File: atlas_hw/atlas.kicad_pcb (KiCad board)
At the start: 4 copper layers, 147 parts, among them J1 USB_B_Micro, J10 PSP_LCD, J2 DEBUG_STM, J3 PSP_TOUCH, J4 UPDI_DSS, J5 EXP_L, J6 EXP_R, J8 Micro_SD_Card_Det, J9 PSP_LCD_BL, Q1 Q_NMOS_DGS, Q2 Q_NMOS_DGS, Q4 Q_NMOS_DGS, SW1 BTN_L_EXT, SW2 BTN_0_EXT, SW3 ResetSTM, SW4 BTN_R_EXT, SW5 BTN_PWR_EXT, U1 STM32H723VITx, U11 L96-M33, U13 LSF0108, U14 NPP600SNADJ, U16 PAM2841, U2 S27KL0641DABHV023, U3 MCP1811B, U4 TLV62569DBV, U5 MX25L3233FM2I-08G, U6 ST1PS02, U7 ATtiny402-SS, U9 MC6470, Y1 16M, Y4 32k

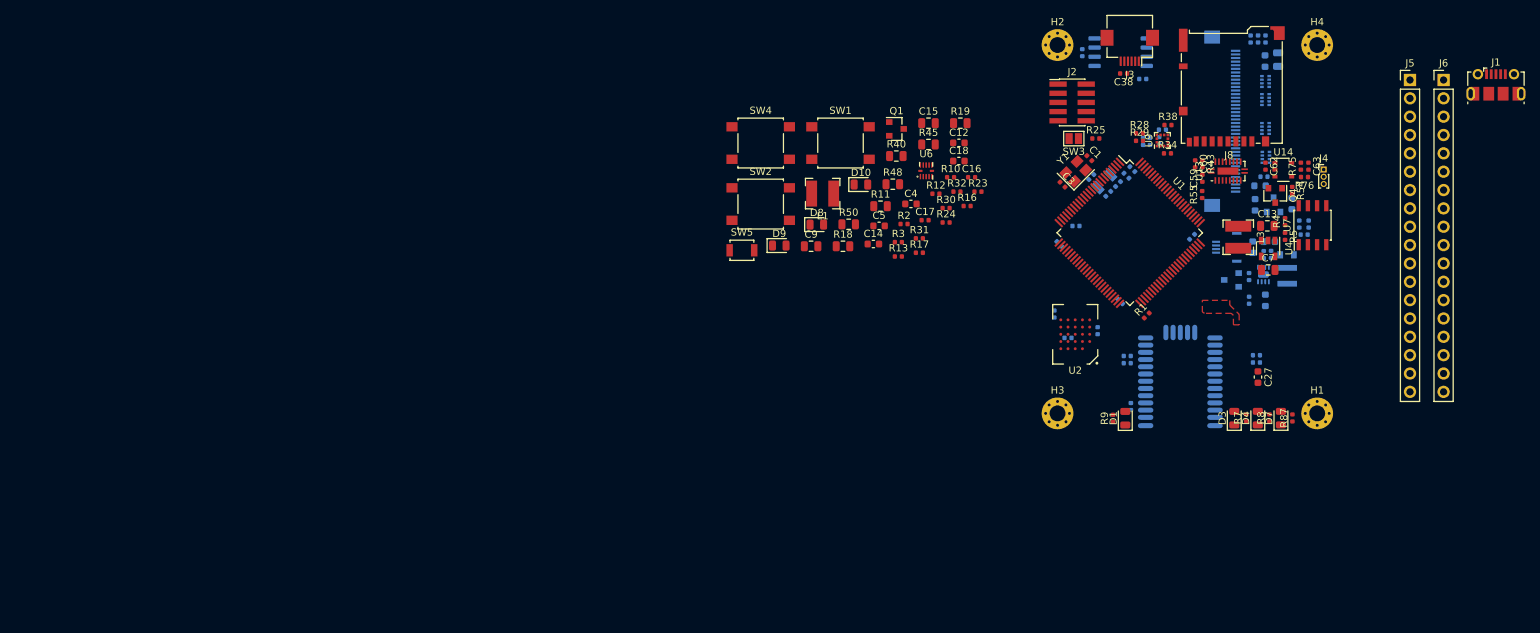
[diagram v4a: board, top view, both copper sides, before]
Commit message: dfm reductions
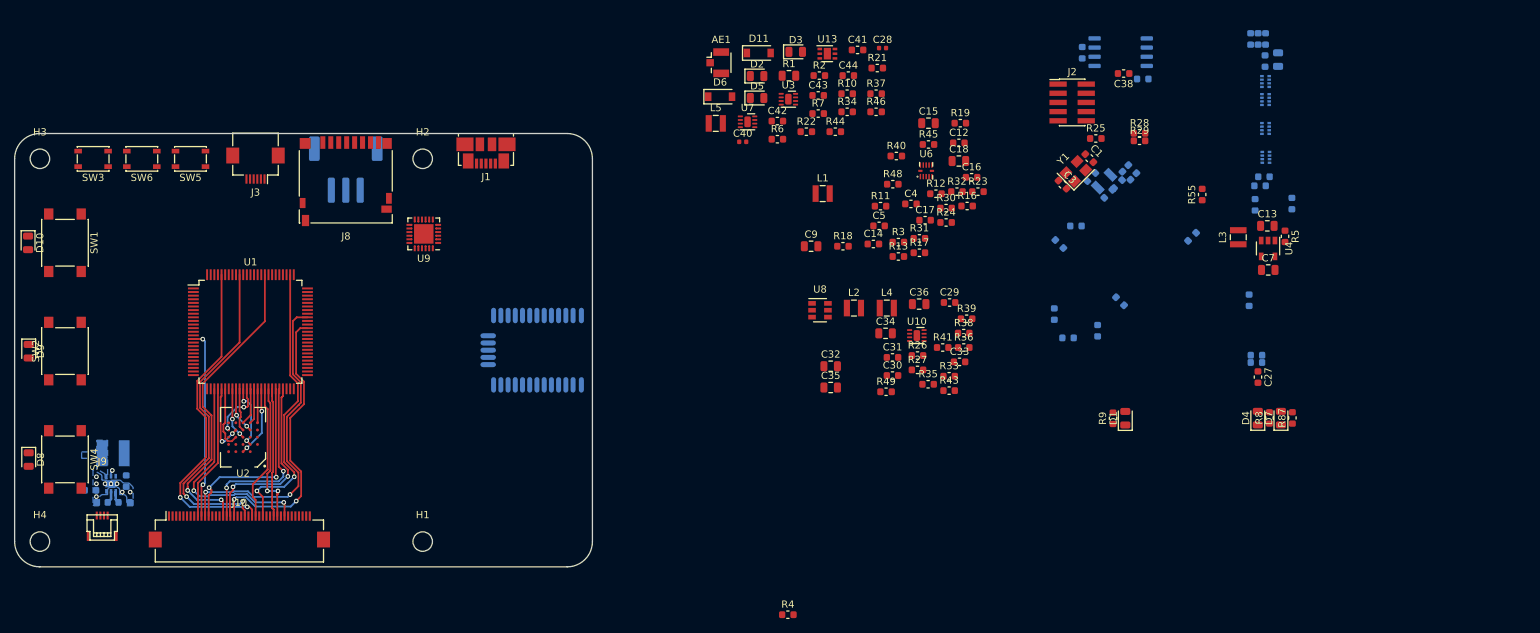
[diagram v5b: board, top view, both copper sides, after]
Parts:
- removed C48: 1u, Capacitor_SMD:C_0603_1608Metric
- removed C49, C59, C60: 0.1u, Capacitor_SMD:C_0402_1005Metric
- removed C62, C63: 1u, Capacitor_SMD:C_0402_1005Metric
- removed J4: UPDI_DSS, Connector_PinHeader_1.00mm:PinHeader_1x03_P1.00mm_Vertical
- removed J6: EXP_R, Connector_PinHeader_2.54mm:PinHeader_1x18_P2.54mm_Vertical
- removed Q1, Q2, Q4: Q_NMOS_DGS, Package_TO_SOT_SMD:SOT-23
- removed R50: 100k, Resistor_SMD:R_0805_2012Metric
- removed R54: 10k, Resistor_SMD:R_0402_1005Metric
- removed R75: 200k, Resistor_SMD:R_0402_1005Metric
- removed R76: 250k, Resistor_SMD:R_0402_1005Metric
- removed R78, R79: 4.7k, Resistor_SMD:R_0402_1005Metric
- removed U14: NPP600SNADJ, Package_SO:TSOP-5_1.65x3.05mm_P0.95mm
- removed U16: PAM2841, Package_DFN_QFN:DFN-8-1EP_2x2mm_P0.5mm_EP0.9x1.5mm
- added AE1: Antenna_Shield, Connector_Coaxial:U.FL_Hirose_U.FL-R-SMT-1_Vertical, F.Cu at (131.0, 90.2)
- added C29: 1u, Capacitor_SMD:C_0603_1608Metric, F.Cu at (163.1, 123.4)
- added C30: 1u, Capacitor_SMD:C_0603_1608Metric, F.Cu at (155.2, 133.5)
- added C31: 1u, Capacitor_SMD:C_0603_1608Metric, F.Cu at (155.2, 131.0)
- added C33: 0.1u, Capacitor_SMD:C_0603_1608Metric, F.Cu at (164.5, 131.6)
- added C35: 10u, Capacitor_SMD:C_0805_2012Metric, F.Cu at (146.6, 135.2)
- added C36: 10u, Capacitor_SMD:C_0805_2012Metric, F.Cu at (158.9, 123.6)
- added C37: 1u, Capacitor_SMD:C_0603_1608Metric, B.Cu at (49.1, 148.1)
- added C39: 0.1u, Capacitor_SMD:C_0603_1608Metric, B.Cu at (45.8, 151.1)
- added C40: NP, Capacitor_SMD:C_0402_1005Metric, F.Cu at (134.5, 101.2)
- added C41: 4.7u, Capacitor_SMD:C_0603_1608Metric, F.Cu at (150.4, 88.4)
- added C42: 1u, Capacitor_SMD:C_0603_1608Metric, F.Cu at (139.3, 98.3)
- added C43: 1u, Capacitor_SMD:C_0603_1608Metric, F.Cu at (144.9, 94.7)
- added C44: 1u, Capacitor_SMD:C_0603_1608Metric, F.Cu at (149.1, 92.0)
- added D11: MBR0540, Diode_SMD:D_SOD-123, F.Cu at (136.7, 88.8)
- added D2: GPS_3DF, LED_SMD:LED_0805_2012Metric, F.Cu at (136.4, 92.0)
- added D5: GPS_JAM, LED_SMD:LED_0805_2012Metric, F.Cu at (136.4, 95.1)
- added L2: 2.2u, Inductor_SMD:L_Wuerth_MAPI-2510, F.Cu at (149.9, 124.2)
- added L4: 2.2u, Inductor_SMD:L_Wuerth_MAPI-2510, F.Cu at (154.4, 124.2)
- added L5: 47n, Inductor_SMD:L_Wuerth_MAPI-2510, F.Cu at (130.7, 98.6)
- added R33: 0, Resistor_SMD:R_0603_1608Metric, F.Cu at (163.0, 133.6)
- added R35: 100k, Resistor_SMD:R_0603_1608Metric, F.Cu at (160.1, 134.7)
- added R36: 100k, Resistor_SMD:R_0603_1608Metric, F.Cu at (165.1, 129.6)
- added R37: 440k, Resistor_SMD:R_0603_1608Metric, F.Cu at (152.9, 94.5)
- added R41: 0, Resistor_SMD:R_0603_1608Metric, F.Cu at (162.2, 129.6)
- added R46: 100k, Resistor_SMD:R_0603_1608Metric, F.Cu at (152.9, 97.0)
- added R49: 100k, Resistor_SMD:R_0603_1608Metric, F.Cu at (154.3, 135.8)
- added SW6: BTN_BOOT, Button_Switch_SMD:SW_SPST_PTS810, F.Cu at (51.3, 103.5)
- added U10: MAX17048, Package_DFN_QFN:DFN-8-1EP_2x2mm_P0.5mm_EP0.9x1.5mm, F.Cu at (158.6, 128.0)
- added U12: LV52204MU, Package_DFN_QFN:DFN-6-1EP_2x2mm_P0.65mm_EP1x1.6mm, B.Cu at (47.0, 148.5)
- added U8: MCP1640B, Package_TO_SOT_SMD:SOT-23-6, F.Cu at (145.2, 124.5)
- C1, C11, C16, C17, C2, C22, C23, C24, C25, C26, C3, C38, C54, C56, C57, C58, C6: footprint Capacitor_SMD:C_0402_1005Metric -> Capacitor_SMD:C_0603_1608Metric
- C18: footprint Capacitor_SMD:C_0603_1608Metric -> Capacitor_SMD:C_0805_2012Metric
- C19, C21: value 22p -> 18p; footprint Capacitor_SMD:C_0402_1005Metric -> Capacitor_SMD:C_0603_1608Metric
- C28: value 0.1u -> NP; moved to F.Cu
- C32: value 0.1u -> 10u; footprint Capacitor_SMD:C_0402_1005Metric -> Capacitor_SMD:C_0805_2012Metric; moved to F.Cu
- C34: value 0.1u -> 4.7u; footprint Capacitor_SMD:C_0402_1005Metric -> Capacitor_SMD:C_0805_2012Metric; moved to F.Cu
- C7: value 10u -> 4.7u
- C8: value 1u -> 4.7u
- D3: value GPS_3DF -> CHG_STATUS
- D6: value D_Schottky_Small_ALT -> MBR0540; footprint Diode_SMD:D_SOD-110 -> Diode_SMD:D_SOD-123; moved to F.Cu
- H1, H2, H3, H4: value MountingHole_Pad -> MountingHole; footprint MountingHole:MountingHole_2.2mm_M2_Pad_Via -> MountingHole:MountingHole_2.7mm_M2.5
- J1: footprint Connector_USB:USB_Micro-B_Molex-105017-0001 -> Connector_USB:USB_Micro-B_Molex_47346-0001
- J10, J9: moved to F.Cu
- J5: value EXP_L -> CELL; footprint Connector_PinHeader_2.54mm:PinHeader_1x18_P2.54mm_Vertical -> Connector_JST:JST_PH_S3B-PH-SM4-TB_1x03-1MP_P2.00mm_Horizontal; moved to B.Cu
- J8: footprint Connector_Card:microSD_HC_Hirose_DM3BT-DSF-PEJS -> Connector_Card:microSD_HC_Hirose_DM3D-SF
- L1: footprint Inductor_SMD:L_Bourns-SRN4018 -> Inductor_SMD:L_Wuerth_MAPI-2510
- L10: value 3.9n -> 22u; footprint Inductor_SMD:L_Taiyo-Yuden_MD-3030 -> Inductor_SMD:L_Bourns-SRN4018
- L3: value L_Small -> 2.2u; footprint Inductor_SMD:L_Bourns-SRN4018 -> Inductor_SMD:L_Wuerth_MAPI-2510
- R1: value 100k -> 0; footprint Resistor_SMD:R_0402_1005Metric -> Resistor_SMD:R_0805_2012Metric
- R10: value 100k -> NP; footprint Resistor_SMD:R_0402_1005Metric -> Resistor_SMD:R_0603_1608Metric
- R11, R18, R19, R40, R45, R48: footprint Resistor_SMD:R_0805_2012Metric -> Resistor_SMD:R_0603_1608Metric
- R12, R13, R14, R15, R16, R17, R23, R24, R25, R30, R31, R32, R34, R42, R47, R5, R55, R7, R8, R82, R83, R84, R87, R9: footprint Resistor_SMD:R_0402_1005Metric -> Resistor_SMD:R_0603_1608Metric
- R2: value 100k -> 1k; footprint Resistor_SMD:R_0402_1005Metric -> Resistor_SMD:R_0603_1608Metric
- R21: footprint Resistor_SMD:R_0402_1005Metric -> Resistor_SMD:R_0603_1608Metric; moved to F.Cu
- R22: value 0 -> 100k; footprint Resistor_SMD:R_0402_1005Metric -> Resistor_SMD:R_0603_1608Metric; moved to F.Cu
- R26: value NP -> 450; footprint Resistor_SMD:R_0402_1005Metric -> Resistor_SMD:R_0603_1608Metric; moved to F.Cu
- R27: value NP -> 240; footprint Resistor_SMD:R_0402_1005Metric -> Resistor_SMD:R_0603_1608Metric; moved to F.Cu
- R28, R29: value 4.7k -> 5.7k; footprint Resistor_SMD:R_0402_1005Metric -> Resistor_SMD:R_0603_1608Metric
- R3, R43: value 100k -> 0; footprint Resistor_SMD:R_0402_1005Metric -> Resistor_SMD:R_0603_1608Metric
- R38: value 100k -> 5.7k; footprint Resistor_SMD:R_0402_1005Metric -> Resistor_SMD:R_0603_1608Metric
- R39: value 0 -> 30k; footprint Resistor_SMD:R_0402_1005Metric -> Resistor_SMD:R_0603_1608Metric; moved to F.Cu
- R4: value 200k -> 100k; footprint Resistor_SMD:R_0402_1005Metric -> Resistor_SMD:R_0603_1608Metric
- R44: value 100k -> 10; footprint Resistor_SMD:R_0402_1005Metric -> Resistor_SMD:R_0603_1608Metric; moved to F.Cu
- R6: value 100k -> 1k; footprint Resistor_SMD:R_0402_1005Metric -> Resistor_SMD:R_0603_1608Metric; moved to F.Cu
- SW1: value BTN_L_EXT -> BTN_L; footprint Button_Switch_SMD:SW_SPST_B3S-1000 -> Button_Switch_SMD:SW_SPST_PTS645
- SW2: value BTN_0_EXT -> BTN_0; footprint Button_Switch_SMD:SW_SPST_B3S-1000 -> Button_Switch_SMD:SW_SPST_PTS645
- SW3: footprint Jumper:SolderJumper-2_P1.3mm_Open_Pad1.0x1.5mm -> Button_Switch_SMD:SW_SPST_PTS810
- SW4: value BTN_R_EXT -> BTN_R; footprint Button_Switch_SMD:SW_SPST_B3S-1000 -> Button_Switch_SMD:SW_SPST_PTS645
- SW5: value BTN_PWR_EXT -> BTN_PWR; footprint Button_Switch_SMD:SW_SPST_B3U-1000P -> Button_Switch_SMD:SW_SPST_PTS810
- U1: value STM32H723VITx -> STM32H723VGT6
- U13: value LSF0108 -> AP22804; footprint Package_DFN_QFN:WQFN-20-1EP_2.5x4.5mm_P0.5mm_EP1x2.9mm -> Package_DFN_QFN:DFN-6-1EP_2x2mm_P0.65mm_EP1x1.6mm
- U3: value MCP1811B -> MCP1810; footprint Package_TO_SOT_SMD:SOT-23 -> Package_DFN_QFN:DFN-8-1EP_2x2mm_P0.5mm_EP0.9x1.5mm; moved to F.Cu
- U7: value ATtiny402-SS -> MCP1810; footprint Package_SO:SOIC-8_3.9x4.9mm_P1.27mm -> Package_DFN_QFN:DFN-8-1EP_2x2mm_P0.5mm_EP0.9x1.5mm
- U9: value MC6470 -> BQ25606; footprint Package_LGA:LGA-12_2x2mm_P0.5mm -> Package_DFN_QFN:WQFN-24-1EP_4x4mm_P0.5mm_EP2.7x2.7mm
- Y1: value 16M -> 8M
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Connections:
- net /DSS_EXT renamed Net-(U7-Pad5)
- C1 pad 1: GND -> EP
- C10 pad 1: GND -> EP
- C11 pad 1: /VCC_3V3 -> Net-(C11-Pad1)
- C11 pad 2: GND -> EP
- C12 pad 2: GND -> EP
- C13 pad 1: /VCC_3V3 -> /VCC_3V3_MCU
- C13 pad 2: GND -> EP
- C14 pad 2: GND -> EP
- C15 pad 2: GND -> EP
- C16 pad 2: GND -> EP
- C17 pad 2: GND -> EP
- C18 pad 2: GND -> EP
- C19 pad 1: GND -> EP
- C2 pad 1: GND -> EP
- C2 pad 2: /VCC_3V3 -> /VCC_3V3_PERIPH
- C20 pad 1: /VCC_MCU_3V3 -> /VCC_3V3_PERIPH
- C20 pad 2: GND -> EP
- C21 pad 1: GND -> EP
- C22 pad 1: /VCC_3V3 -> /VCC_3V3_MCU
- C22 pad 2: GND -> EP
- C23 pad 1: /VCC_3V3 -> /VCC_3V3_MCU
- C23 pad 2: GND -> EP
- C24 pad 1: /VCC_3V3 -> /VCC_3V3_MCU
- C24 pad 2: GND -> EP
- C25 pad 1: /VCC_3V3 -> /VCC_3V3_MCU
- C25 pad 2: GND -> EP
- C26 pad 1: /VCC_3V3 -> /VCC_3V3_MCU
- C26 pad 2: GND -> EP
- C27 pad 2: GND -> EP
- C28 pad 1: GND -> EP
- C28 pad 2: /VCC_BACKUP -> Net-(C28-Pad2)
- C3 pad 1: GND -> EP
- C32 pad 1: /VCC_3V3 -> Net-(C32-Pad1)
- C32 pad 2: GND -> EP
- C34 pad 1: /VCC_3V3 -> Net-(C34-Pad1)
- C34 pad 2: GND -> EP
- C38 pad 1: /VCC_MCU_3V3 -> /VCC_3V3_PERIPH
- C38 pad 2: GND -> EP
- C4 pad 2: GND -> EP
- C5 pad 2: GND -> EP
- C51 pad 1: /VCC_SYS -> /VCC_LCD_PWR
- C51 pad 2: GND -> EP
- C52 pad 1: GND -> EP
- C52 pad 2: Net-(C52-Pad2) -> /BL_HV
- C53 pad 1: /VCC_SYS -> /VCC_LCD_PWR
- C53 pad 2: GND -> EP
- C54 pad 1: /VCC_MCU_3V3 -> /VCC_3V3_PERIPH
- C54 pad 2: GND -> EP
- C56 pad 1: GND -> EP
- C56 pad 2: /VCC_3V3 -> /VCC_3V3_PERIPH
- C57 pad 1: GND -> EP
- C57 pad 2: /VCC_3V3 -> /VCC_3V3_PERIPH
- C58 pad 1: GND -> EP
- C58 pad 2: /VCC_3V3 -> /VCC_3V3_PERIPH
- C6 pad 2: GND -> EP
- C7 pad 2: GND -> EP
- C8 pad 1: GND -> EP
- C9 pad 1: /VCC_SYS -> Net-(C9-Pad1)
- C9 pad 2: GND -> EP
- D10 pad 1: GND -> EP
- D3 pad 2: /GPS_3DF -> /VCC_BACKUP
- D6 pad 1: Net-(C52-Pad2) -> /VCC_3V3_MCU_EN
- D6 pad 2: Net-(D6-Pad2) -> /SW_PWR
- D8 pad 1: GND -> EP
- D9 pad 1: GND -> EP
- H1 pad 1: GND -> (no net)
- H2 pad 1: GND -> (no net)
- H3 pad 1: GND -> (no net)
- H4 pad 1: GND -> (no net)
- J1 pad 2: /USB_PORT_D- -> /USB_PORT_D+
- J1 pad 3: /USB_PORT_D+ -> /USB_PORT_D-
- J1 pad 5: GND -> EP
- J1 pad 6: GND -> EP
- J10 pad 35: /VCC_SYS -> /VCC_LCD_PWR
- J10 pad 36: /VCC_SYS -> /VCC_LCD_PWR
- J2 pad 1: /VCC_3V3 -> /VCC_3V3_MCU
- J2 pad 3: GND -> EP
- J2 pad 5: GND -> EP
- J2 pad 9: GND -> EP
- J3 pad 1: /I2C1_SCL_SENSOR -> /I2C4_SCL_SENSOR_PB6
- J3 pad 2: /I2C1_SDA_SENSOR -> /I2C4_SCL_SENSOR_PB7
- J3 pad 3: /STC911_INT -> /TOUCH_INT
- J3 pad 6: /STC911_RESET -> /DEBUG_NRESET_STM
- J5 pad 1: /USB_PORT_VBUS -> GND
- J5 pad 2: /VCC_SYS -> /CELL_NTC
- J5 pad 3: /VCC_BACKUP -> /CELL_POS
- J8 pad 10: GND -> /SD_DET
- J8 pad 9: /SD_DET -> GND
- J9 pad 1: Net-(C52-Pad2) -> /BL_HV
- L10 pad 2: Net-(D6-Pad2) -> Net-(D11-Pad2)
- L3 pad 2: /VCC_3V3 -> /VCC_3V3_MCU
- R1 pad 1: /VCC_MCU_3V3 -> Net-(C11-Pad1)
- R1 pad 2: /PWR_ACK_DSS -> /VCC_3V3_MCU
- R10 pad 1: /STM_VCORE_GOOD -> /VCC_SYS
- R10 pad 2: /VCC_MCU_3V3 -> Net-(C9-Pad1)
- R14 pad 1: /USB_STM_D+ -> /USB_STM_D-
- R14 pad 2: /USB_PORT_D+ -> /USB_PORT_D-
- R15 pad 1: /USB_STM_D- -> /USB_STM_D+
- R15 pad 2: /USB_PORT_D- -> /USB_PORT_D+
- R18 pad 1: /STM_STATUS_0 -> /STM_STATUS_C
- R2 pad 1: /PWR_EN_O -> Net-(D2-Pad1)
- R2 pad 2: /VCORE_EN -> EP
- R21 pad 1: Net-(R21-Pad1) -> /VCC_3V3_MCU
- R21 pad 2: /VCC_MCU_3V3 -> Net-(C9-Pad1)
- R22 pad 1: Net-(R21-Pad1) -> /SW_PWR
- R22 pad 2: /DEBUG_NRESET_STM -> EP
- R25 pad 2: /VCC_3V3 -> /VCC_3V3_MCU
- R26 pad 1: GND -> Net-(R26-Pad1)
- R26 pad 2: Net-(R26-Pad2) -> EP
- R27 pad 1: Net-(R26-Pad2) -> Net-(R27-Pad1)
- R27 pad 2: /VCC_MCU_3V3 -> EP
- R28 pad 1: /VCC_MCU_3V3 -> /VCC_3V3_PERIPH
- R28 pad 2: /I2C1_SCL_SENSOR -> /I2C4_SCL_SENSOR_PB6
- R29 pad 1: /VCC_MCU_3V3 -> /VCC_3V3_PERIPH
- R29 pad 2: /I2C1_SDA_SENSOR -> /I2C4_SCL_SENSOR_PB7
- R3 pad 1: GND -> EP
- R34 pad 1: /VCC_MCU_3V3 -> /STM_VCORE_GOOD
- R34 pad 2: /MC6470_INTA -> /VCC_CORE
- R38 pad 1: /VCC_MCU_3V3 -> Net-(C34-Pad1)
- R38 pad 2: /MC6470_INTM -> /CELL_NTC
- R39 pad 1: Net-(R39-Pad1) -> /CELL_NTC
- R39 pad 2: Net-(R39-Pad2) -> EP
- R4 pad 1: Net-(R4-Pad1) -> /VCC_3V3
- R4 pad 2: /VCC_3V3 -> /SW_BOOT
- R42 pad 1: /VCC_MCU_3V3 -> /VCC_3V3_PERIPH
- R42 pad 2: /STC911_INT -> /TOUCH_INT
- R43 pad 1: /VDD_SD_IO_3V3_1V8 -> /USB_CHG_D+
- R43 pad 2: Net-(R43-Pad2) -> /USB_PORT_D+
- R44 pad 1: /VCC_BACKUP -> Net-(C42-Pad2)
- R44 pad 2: /PWR_EN_O -> Net-(L5-Pad2)
- R45 pad 2: /SW_0 -> /SW_C
- R47 pad 1: GND -> EP
- R47 pad 2: /EN_LCD_PWR -> /T3C1_LCD_BL
- R5 pad 1: GND -> EP
- R5 pad 2: Net-(R4-Pad1) -> Net-(R37-Pad1)
- R55 pad 2: /VCC_MCU_3V3 -> /VCC_3V3_PERIPH
- R6 pad 1: /PWR_EN_O -> Net-(D3-Pad1)
- R6 pad 2: GND -> /CHG_STATUS
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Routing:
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- added copper zone on B.Cu, net EP
- added copper zone on B.Cu, net Net-(D11-Pad2)
- removed copper zone on F.Cu, net Net-(C41-Pad1)
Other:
- board outline added: 80 x 60 mm

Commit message: lots of modifications to sch and board
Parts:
- added C45: 10u, Capacitor_SMD:C_0805_2012Metric, B.Cu at (90.2, 143.0)
- added C46: 0.1u, Capacitor_SMD:C_0402_1005Metric, F.Cu at (180.4, 122.1)
- added C47: 0.1u, Capacitor_SMD:C_0402_1005Metric, F.Cu at (188.3, 119.1)
- added C48: 0.1u, Capacitor_SMD:C_0402_1005Metric, F.Cu at (136.6, 93.7)
- added C49: 1u, Capacitor_SMD:C_0603_1608Metric, F.Cu at (143.0, 81.3)
- added C50: 1u, Capacitor_SMD:C_0603_1608Metric, F.Cu at (137.7, 89.2)
- added C55: 1u, Capacitor_SMD:C_0603_1608Metric, F.Cu at (125.8, 92.5)
- added C59: 0.1u, Capacitor_SMD:C_0402_1005Metric, F.Cu at (143.0, 83.3)
- added C60: 0.1u, Capacitor_SMD:C_0402_1005Metric, F.Cu at (133.7, 93.7)
- added C61: 0.1u, Capacitor_SMD:C_0402_1005Metric, F.Cu at (136.6, 91.7)
- added C62: 10n, Capacitor_SMD:C_0402_1005Metric, F.Cu at (143.0, 85.3)
- added C63: 0.1u, Capacitor_SMD:C_0402_1005Metric, F.Cu at (140.6, 89.2)
- added C64: 0.1u, Capacitor_SMD:C_0402_1005Metric, F.Cu at (133.7, 91.7)
- added C65: 0.1u, Capacitor_SMD:C_0402_1005Metric, F.Cu at (139.5, 91.2)
- added J4: DEBUG_NCP, Connector_PinHeader_1.27mm:PinHeader_2x05_P1.27mm_Vertical_SMD, B.Cu at (47.1, 151.5)
- added JP2: Jumper_NO_Small, Connector_PinHeader_1.00mm:PinHeader_1x02_P1.00mm_Vertical, F.Cu at (135.2, 53.4)
- added L6: FERRITE, Inductor_SMD:L_0603_1608Metric, F.Cu at (140.4, 148.8)
- added R50: 0, Resistor_SMD:R_0402_1005Metric, F.Cu at (99.1, 115.4)
- added R51: 0, Resistor_SMD:R_0402_1005Metric, F.Cu at (109.4, 122.5)
- added RV1: 200k, Potentiometer_SMD:Potentiometer_Bourns_3314J_Vertical, F.Cu at (136.6, 48.1)
- added SW7: NP, Button_Switch_SMD:SW_SPST_PTS645, F.Cu at (43.3, 129.9)
- added TP1: VCC_CORE, TestPoint:TestPoint_Bridge_Pitch2.0mm_Drill0.7mm, F.Cu at (172.2, 119.3)
- added U14: MS5637, atlas:QFN-4_3x3_Pitch2mm, F.Cu at (61.7, 115.6)
- added U15: SHT4x, atlas:SHT_QFN-4-1EP_1.5x1.5mm, F.Cu at (61.8, 110.8)
- added U16: PSP_JOY, atlas:PSP-JOY, F.Cu at (43.2, 130.0)
- added U17: BGM220P, atlas:BGM220P, B.Cu at (41.6, 130.0)
- added U18: FXOS8700CQ, atlas:LGA-16_3x3mm_P0.5mm_LayoutBorder3x5y, B.Cu at (55.2, 113.2)
- added U19: L2G2IS, atlas:LGA-16_2.3x2.3mm_P0.4mm_LayoutBorder3x5y, B.Cu at (48.0, 113.2)
- added U20: AZ2117, Package_TO_SOT_SMD:SOT-223-3_TabPin2, F.Cu at (62.0, 80.1)
- C1, C13, C3, C35, C36, C42, C43, C7, D11, J1, J2, L1, L2, L3, L4, R3, R34, R36, R37, R41, R43, R44, R5, U10, U13, U2, U3, U4, U6, U7, U8, U9: moved to B.Cu
- C11, C22, C23, C24, C25, C26, C56, C57, C58, C6: footprint Capacitor_SMD:C_0603_1608Metric -> Capacitor_SMD:C_0402_1005Metric; moved to F.Cu
- C16, C17, C2, C38, C39, C54: footprint Capacitor_SMD:C_0603_1608Metric -> Capacitor_SMD:C_0402_1005Metric
- C19, C21, R14, R15, U11: moved to F.Cu
- C29: value 1u -> 10u; footprint Capacitor_SMD:C_0603_1608Metric -> Capacitor_SMD:C_0805_2012Metric
- C30: value 1u -> 0.1u; footprint Capacitor_SMD:C_0603_1608Metric -> Capacitor_SMD:C_0402_1005Metric
- C31: value 1u -> 4.7u; footprint Capacitor_SMD:C_0603_1608Metric -> Capacitor_SMD:C_0805_2012Metric; moved to B.Cu
- C33: footprint Capacitor_SMD:C_0603_1608Metric -> Capacitor_SMD:C_0402_1005Metric; moved to B.Cu
- C41: footprint Capacitor_SMD:C_0603_1608Metric -> Capacitor_SMD:C_0805_2012Metric; moved to B.Cu
- C44: value 1u -> 10u; footprint Capacitor_SMD:C_0603_1608Metric -> Capacitor_SMD:C_0805_2012Metric; moved to B.Cu
- C8: footprint Capacitor_SMD:C_0603_1608Metric -> Capacitor_SMD:C_0805_2012Metric
- D5: value GPS_JAM -> NP
- D9: value STM_STATUS_0 -> PERIPH_FAULT
- H1, H2, H3, H4: footprint MountingHole:MountingHole_2.7mm_M2.5 -> MountingHole:MountingHole_2.7mm_M2.5_Pad_Via
- J5: footprint Connector_JST:JST_PH_S3B-PH-SM4-TB_1x03-1MP_P2.00mm_Horizontal -> Connector_PinHeader_1.27mm:PinHeader_1x03_P1.27mm_Vertical
- L5: footprint Inductor_SMD:L_Wuerth_MAPI-2510 -> Inductor_SMD:L_0402_1005Metric; moved to B.Cu
- R1: value 0 -> 1k; footprint Resistor_SMD:R_0805_2012Metric -> Resistor_SMD:R_0603_1608Metric
- R16: value 0 -> 100k
- R18: value 1k -> NP
- R26: value 450 -> 1k
- R27: value 240 -> 1k
- R28, R29, R38: value 5.7k -> 5.23k
- R33: value 0 -> NP
- R35: value 100k -> 316k; moved to B.Cu
- R46: value 100k -> 0; footprint Resistor_SMD:R_0603_1608Metric -> Resistor_SMD:R_0402_1005Metric
- R7: value 1k -> 100k
- SW2: value BTN_0 -> ResetNCP; moved to B.Cu
- SW3, SW6: footprint Button_Switch_SMD:SW_SPST_PTS810 -> Button_Switch_SMD:SW_SPST_PTS645; moved to B.Cu
- SW5: footprint Button_Switch_SMD:SW_SPST_PTS810 -> Button_Switch_SMD:SW_SPST_PTS645
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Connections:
- net /PE0 renamed /SPI4_NCS_ACCEL
- net /PE1 renamed /SPI4_NCS_GYRO
- AE1 pad 2: EP -> GND
- C1 pad 1: EP -> GND
- C10 pad 1: EP -> GND
- C11 pad 2: EP -> GND
- C12 pad 2: EP -> GND
- C13 pad 2: EP -> GND
- C14 pad 2: EP -> GND
- C15 pad 2: EP -> GND
- C16 pad 2: EP -> GND
- C17 pad 2: EP -> GND
- C18 pad 2: EP -> GND
- C19 pad 1: EP -> GND
- C2 pad 1: EP -> GND
- C20 pad 2: EP -> GND
- C21 pad 1: EP -> GND
- C22 pad 2: EP -> GND
- C23 pad 2: EP -> GND
- C24 pad 2: EP -> GND
- C25 pad 2: EP -> GND
- C26 pad 2: EP -> GND
- C27 pad 2: EP -> GND
- C28 pad 1: EP -> Net-(C28-Pad1)
- C28 pad 2: Net-(C28-Pad2) -> GND
- C29 pad 1: EP -> /USB_PORT_VBUS
- C29 pad 2: /VCC_SYS -> GND
- C3 pad 1: EP -> GND
- C30 pad 1: EP -> /CELL_POS
- C30 pad 2: /VCC_LCD_PWR -> GND
- C31 pad 1: EP -> GND
- C31 pad 2: Net-(C31-Pad2) -> /USB_PORT_VBUS
- C32 pad 2: EP -> GND
- C34 pad 2: EP -> GND
- C35 pad 1: /VCC_SYS -> /USB_PORT_VBUS
- C35 pad 2: EP -> GND
- C36 pad 2: EP -> GND
- C37 pad 1: EP -> GND
- C37 pad 2: /VCC_SYS -> /USB_PORT_VBUS
- C38 pad 2: EP -> GND
- C39 pad 2: EP -> GND
- C4 pad 2: EP -> GND
- C40 pad 2: EP -> GND
- C41 pad 1: EP -> GND
- C42 pad 1: EP -> GND
- C43 pad 1: EP -> GND
- C44 pad 1: EP -> GND
- C5 pad 2: EP -> GND
- C51 pad 2: EP -> GND
- C52 pad 1: EP -> GND
- C53 pad 2: EP -> GND
- C54 pad 2: EP -> GND
- C56 pad 1: EP -> GND
- C57 pad 1: EP -> GND
- C58 pad 1: EP -> GND
- C6 pad 2: EP -> GND
- C7 pad 1: /VCC_SYS -> /USB_PORT_VBUS
- C7 pad 2: EP -> GND
- C8 pad 1: EP -> GND
- C8 pad 2: /VCC_SYS -> /USB_PORT_VBUS
- C9 pad 2: EP -> GND
- D10 pad 1: EP -> GND
- D5 pad 1: Net-(D5-Pad1) -> GND
- D5 pad 2: /VCC_3V3_PERIPH -> Net-(D5-Pad2)
- D8 pad 1: EP -> GND
- D9 pad 1: EP -> Net-(D9-Pad1)
- D9 pad 2: Net-(D9-Pad2) -> /VCC_3V3_MCU
- H1 pad 1: (no net) -> GND
- H2 pad 1: (no net) -> GND
- H3 pad 1: (no net) -> GND
- H4 pad 1: (no net) -> GND
- J1 pad 5: EP -> GND
- J1 pad 6: EP -> GND
- J10 pad 1: GND -> Net-(J10-Pad1)
- J10 pad 10: /LTDC_R5 -> /LTDC_DE
- J10 pad 11: /LTDC_R6 -> /LTDC_CK
- J10 pad 12: /LTDC_R7 -> GND
- J10 pad 13: /LTDC_G4 -> /LTDC_B7
- J10 pad 14: /LTDC_G5 -> /LTDC_B6
- J10 pad 15: /LTDC_G6 -> /LTDC_B5
- J10 pad 16: /LTDC_G7 -> /LTDC_B4
- J10 pad 17: /LTDC_G4 -> /LTDC_B7
- J10 pad 18: /LTDC_G5 -> /LTDC_B6
- J10 pad 19: /LTDC_G6 -> /LTDC_B5
- J10 pad 2: GND -> Net-(J10-Pad2)
- J10 pad 20: /LTDC_G7 -> /LTDC_B4
- J10 pad 21: /LTDC_B4 -> /LTDC_G7
- J10 pad 22: /LTDC_B5 -> /LTDC_G6
- J10 pad 23: /LTDC_B6 -> /LTDC_G5
- J10 pad 24: /LTDC_B7 -> /LTDC_G4
- J10 pad 25: /LTDC_B4 -> /LTDC_G7
- J10 pad 26: /LTDC_B5 -> /LTDC_G6
- J10 pad 27: /LTDC_B6 -> /LTDC_G5
- J10 pad 28: /LTDC_B7 -> /LTDC_G4
- J10 pad 29: GND -> /LTDC_R7
- J10 pad 3: /VCC_MCU_3V3 -> Net-(J10-Pad3)
- J10 pad 30: /LTDC_CK -> /LTDC_R6
- J10 pad 31: /LTDC_DE -> /LTDC_R5
- J10 pad 32: /LTDC_HS -> /LTDC_R4
- J10 pad 33: /LTDC_VS -> /LTDC_R7
- J10 pad 34: Net-(J10-Pad34) -> /LTDC_R6
- J10 pad 35: /VCC_LCD_PWR -> /LTDC_R5
- J10 pad 36: /VCC_LCD_PWR -> /LTDC_R4
- J10 pad 37: Net-(J10-Pad37) -> /VCC_3V3_PERIPH
- J10 pad 38: Net-(J10-Pad38) -> /VCC_3V3_PERIPH
- J10 pad 39: Net-(J10-Pad39) -> GND
- J10 pad 4: /VCC_MCU_3V3 -> Net-(J10-Pad4)
- J10 pad 40: Net-(J10-Pad40) -> GND
- J10 pad 5: /LTDC_R4 -> /VCC_LCD_PWR
- J10 pad 6: /LTDC_R5 -> /VCC_LCD_PWR
- J10 pad 7: /LTDC_R6 -> Net-(J10-Pad7)
- J10 pad 8: /LTDC_R7 -> /LTDC_VS
- J10 pad 9: /LTDC_R4 -> /LTDC_HS
- J2 pad 3: EP -> GND
- J2 pad 5: EP -> GND
- J2 pad 9: EP -> GND
- L10 pad 1: /VCC_SYS -> /USB_PORT_VBUS
- L2 pad 1: /VCC_SYS -> /USB_PORT_VBUS
- L4 pad 2: /VCC_SYS -> /USB_PORT_VBUS
- R1 pad 1: Net-(C11-Pad1) -> Net-(D9-Pad1)
- R1 pad 2: /VCC_3V3_MCU -> /PERIPH_FAULT
- R10 pad 1: /VCC_SYS -> /USB_PORT_VBUS
- R16 pad 1: /VCC_SYS -> Net-(R16-Pad1)
- R16 pad 2: /USB_PORT_VBUS -> Net-(JP2-Pad1)
- R18 pad 1: /STM_STATUS_C -> /JOY_Y
- R18 pad 2: Net-(D9-Pad2) -> Net-(D5-Pad2)
- R2 pad 2: EP -> GND
- R20 pad 1: GND -> Net-(J9-Pad4)
- R20 pad 2: Net-(J9-Pad4) -> GND
- R22 pad 2: EP -> GND
- R26 pad 2: EP -> GND
- R27 pad 2: EP -> GND
- R29 pad 2: /I2C4_SCL_SENSOR_PB7 -> /I2C4_SDA_SENSOR_PB7
- R3 pad 1: EP -> GND
- R33 pad 1: /VCC_SYS -> /VCC_3V3_MCU
- R33 pad 2: /VCC_LCD_PWR -> /JOY_X
- R34 pad 2: /VCC_CORE -> Net-(R34-Pad2)
- R36 pad 2: EP -> GND
- R39 pad 2: EP -> GND
- R4 pad 1: /VCC_3V3 -> /VCC_MCU_3V3
- R45 pad 1: /VCC_MCU_3V3 -> Net-(R45-Pad1)
- R45 pad 2: /SW_C -> GND
- R46 pad 1: /PERIPH_FLG -> Net-(R46-Pad1)
- R46 pad 2: /VCC_3V3_MCU -> Net-(R46-Pad2)
- R47 pad 1: EP -> GND
- R5 pad 1: EP -> GND
- R7 pad 1: Net-(D5-Pad1) -> /DEBUG_NRESET_NCP
- R7 pad 2: /GPS_JAM -> /VCC_3V3_MCU
- R8 pad 2: EP -> GND
- R82 pad 1: EP -> GND
- R82 pad 2: Net-(J10-Pad38) -> Net-(J10-Pad3)
- R83 pad 1: EP -> GND
- R83 pad 2: Net-(J10-Pad39) -> Net-(J10-Pad2)
- R84 pad 1: EP -> GND
- R84 pad 2: Net-(J10-Pad40) -> Net-(J10-Pad1)
- R87 pad 2: EP -> GND
- R9 pad 2: EP -> GND
- RN1 pad 5: EP -> GND
- RN1 pad 6: EP -> GND
- RN1 pad 7: EP -> GND
- RN1 pad 8: EP -> GND
- RN2 pad 5: EP -> GND
- RN2 pad 6: EP -> GND
- RN2 pad 7: EP -> GND
- RN2 pad 8: EP -> GND
- RN3 pad 5: EP -> GND
- RN3 pad 6: EP -> GND
- RN3 pad 7: EP -> GND
- RN3 pad 8: EP -> GND
- RN4 pad 5: EP -> GND
- RN4 pad 6: EP -> GND
- RN4 pad 7: EP -> GND
- RN4 pad 8: EP -> GND
- SW1 pad 2: EP -> GND
- SW2 pad 1: /SW_C -> /DEBUG_NRESET_NCP
- SW2 pad 2: EP -> GND
- SW3 pad 2: EP -> GND
- SW4 pad 2: EP -> GND
- SW6 pad 2: EP -> GND
- U1 pad 1: /SPI4_SCK_APP_PE2 -> /SPI4_SCK_APP
- U1 pad 10: EP -> GND
- U1 pad 18: /STM_STATUS_C -> /SW_R
- U1 pad 19: EP -> GND
- U1 pad 22: /SW_C -> /JOY_X
- U1 pad 23: /SW_R -> /JOY_Y
- U1 pad 26: EP -> GND
- U1 pad 4: /SPI4_MISO_APP_PE5 -> /SPI4_MISO_APP
- U1 pad 49: EP -> GND
- U1 pad 5: /SPI4_MOSI_APP_PE6 -> /SPI4_MOSI_APP
- U1 pad 55: /USART3_TX_NCP_PD8 -> /USART3_TX_NCP
- U1 pad 56: /USART3_RX_NCP_PD9 -> /USART3_RX_NCP
- U1 pad 58: /USART3_CTS_NCP_PD11 -> /USART3_CTS_NCP
- U1 pad 59: /USART3_RTS_NCP_PD12 -> /USART3_RTS_NCP
- U1 pad 60: /PD13 -> /STM_VCORE_GOOD
- U1 pad 74: EP -> GND
- U1 pad 85: /PD4 -> /ACCEL_INT2
- U1 pad 86: /PD5 -> /ACCEL_INT1
- U1 pad 92: /I2C4_SCL_SENSOR_PB6 -> /I2C4_SCL_SENSOR
- U1 pad 93: /I2C4_SCL_SENSOR_PB7 -> /I2C4_SDA_SENSOR
- U1 pad 99: EP -> GND
- U10 pad 1: EP -> GND
- U10 pad 4: EP -> GND
- U10 pad 6: EP -> GND
- U10 pad 8: /I2C4_SCL_SENSOR_PB6 -> /I2C4_SDA_SENSOR_PB7
- U10 pad 9: EP -> GND
- U11 pad 10: EP -> GND
- U11 pad 11: EP -> GND
- U11 pad 12: EP -> GND
- U11 pad 13: EP -> GND
- U11 pad 14: EP -> GND
- U11 pad 15: EP -> GND
- U11 pad 16: Net-(JP1-Pad3) -> Net-(R46-Pad1)
- U11 pad 17: Net-(C28-Pad2) -> Net-(R46-Pad2)
- U11 pad 18: EP -> GND
- U11 pad 19: EP -> GND
- U11 pad 20: /GPS_JAM -> Net-(U11-Pad20)
- U11 pad 21: EP -> GND
- U11 pad 22: EP -> GND
- U11 pad 27: EP -> GND
- U11 pad 31: EP -> GND
- U11 pad 4: EP -> GND
- U11 pad 5: EP -> GND
- U12 pad 3: EP -> GND
- U12 pad 6: /VCC_SYS -> /USB_PORT_VBUS
- U12 pad 7: EP -> GND
- U13 pad 2: EP -> GND
- U13 pad 4: /PERIPH_FLG -> /PERIPH_FAULT
- U13 pad 7: EP -> GND
- U2 pad B3: EP -> GND
- U2 pad C1: EP -> GND
- U2 pad E5: EP -> GND
- U3 pad 1: EP -> GND
- U3 pad 7: /VCC_SYS -> /USB_PORT_VBUS
- U3 pad 8: /VCC_SYS -> /USB_PORT_VBUS
- U3 pad 9: EP -> GND
- U4 pad 2: EP -> GND
- U4 pad 4: /VCC_SYS -> /USB_PORT_VBUS
- U5 pad 4: EP -> GND
- U6 pad 1: EP -> GND
- U6 pad 4: EP -> GND
- U7 pad 1: EP -> GND
- U7 pad 9: EP -> GND
- U8 pad 2: EP -> GND
- U8 pad 6: /VCC_SYS -> /USB_PORT_VBUS
- U9 pad 1: Net-(C31-Pad2) -> /USB_PORT_VBUS
- U9 pad 15: /VCC_SYS -> /USB_PORT_VBUS
- U9 pad 16: /VCC_SYS -> /USB_PORT_VBUS
- U9 pad 17: EP -> GND
- U9 pad 24: Net-(C31-Pad2) -> /USB_PORT_VBUS
- U9 pad 25: EP -> GND
- U9 pad 6: EP -> GND
- U9 pad 9: EP -> GND
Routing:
- net /LTDC_HS: track 0.00 -> 32.6 mm, vias 0 -> 1
- net /USB_STM_D-: track 0.00 -> 20.4 mm
- net /LCD_REG_EN: track 0.00 -> 19.7 mm, vias 0 -> 2
- net /USB_STM_D+: track 0.00 -> 19.7 mm
- net Net-(C28-Pad1): track 0.00 -> 12.4 mm
- net /OCTOSPIM_P1_NCS: track 9.82 -> 0.00 mm, vias 2 -> 0
- net /LTDC_R7: track 26.4 -> 35.2 mm
- net /LTDC_CK: track 18.8 -> 27.4 mm, vias 0 -> 1
- net /USB_CHG_D-: track 0.00 -> 8.29 mm
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- added copper zone on B.Cu, net GND
- removed copper zone on B.Cu, net EP

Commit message: final component placement
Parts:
- removed C28, C40: NP, Capacitor_SMD:C_0402_1005Metric
- removed C41: 4.7u, Capacitor_SMD:C_0805_2012Metric
- removed C42, C43, C49, C55: 1u, Capacitor_SMD:C_0603_1608Metric
- removed C44: 10u, Capacitor_SMD:C_0805_2012Metric
- removed C47, C48, C60, C64: 0.1u, Capacitor_SMD:C_0402_1005Metric
- removed C62: 10n, Capacitor_SMD:C_0402_1005Metric
- removed H1, H2: MountingHole, MountingHole:MountingHole_2.7mm_M2.5_Pad_Via
- removed the H3 at (37.1, 103.5)
- removed the H4 at (37.1, 156.5)
- removed J4: DEBUG_NCP, Connector_PinHeader_1.27mm:PinHeader_2x05_P1.27mm_Vertical_SMD
- removed J8: Micro_SD_Card_Det, Connector_Card:microSD_HC_Hirose_DM3D-SF
- removed JP2: Jumper_NO_Small, Connector_PinHeader_1.00mm:PinHeader_1x02_P1.00mm_Vertical
- removed L6: FERRITE, Inductor_SMD:L_0603_1608Metric
- removed R14, R15, R21: 0, Resistor_SMD:R_0603_1608Metric
- removed R16, R22, R34, R45: 100k, Resistor_SMD:R_0603_1608Metric
- removed R17, R23, R24, R30, R31, R32: NP, Resistor_SMD:R_0603_1608Metric
- removed R50: 0, Resistor_SMD:R_0402_1005Metric
- removed RV1: 200k, Potentiometer_SMD:Potentiometer_Bourns_3314J_Vertical
- removed SW6: BTN_BOOT, Button_Switch_SMD:SW_SPST_PTS645
- removed TP1: VCC_CORE, TestPoint:TestPoint_Bridge_Pitch2.0mm_Drill0.7mm
- removed U13: AP22804, Package_DFN_QFN:DFN-6-1EP_2x2mm_P0.65mm_EP1x1.6mm
- removed U15: SHT4x, atlas:SHT_QFN-4-1EP_1.5x1.5mm
- removed U16: PSP_JOY, atlas:PSP-JOY
- removed U17: BGM220P, atlas:BGM220P
- removed U19: L2G2IS, atlas:LGA-16_2.3x2.3mm_P0.4mm_LayoutBorder3x5y
- removed U20: AZ2117, Package_TO_SOT_SMD:SOT-223-3_TabPin2
- added H3: MountingHole, MountingHole:MountingHole_2.7mm_M2.5_Pad_Via, F.Cu at (100.2, 103.1)
- added H3: MountingHole, MountingHole:MountingHole_2.7mm_M2.5_Pad_Via, F.Cu at (37.1, 103.1)
- added H4: MountingHole, MountingHole:MountingHole_2.7mm_M2.5_Pad_Via, F.Cu at (100.2, 147.1)
- added H4: MountingHole, MountingHole:MountingHole_2.7mm_M2.5_Pad_Via, F.Cu at (37.1, 147.1)
- added J6: 47352-1001, atlas:MOLEX_47352-1001, F.Cu at (95.5, 114.3)
- added J7: DEBUG_STM, Connector_PinHeader_1.27mm:PinHeader_2x05_P1.27mm_Vertical_SMD, F.Cu at (99.4, 134.7)
- added Q1: DMC2990UDJ, Package_TO_SOT_SMD:SOT-363_SC-70-6, F.Cu at (59.0, 103.3)
- C1, C10, C13, C2, C20, C3, C31, C33, C35, C36, C37, C39, C45, C51, C52, C53, C54, C7, C8, D11, J1, J2, L1, L10, L2, L3, L4, L5, R20, R35, R36, R37, R41, R42, R43, R44, R47, R5, RN1, RN2, RN3, RN4, U10, U12, U18, U2, U3, U4, U5, U6, U8, U9: moved to F.Cu
- D5: value NP -> STM_STATUS_C
- D9: value PERIPH_FAULT -> NCP_STATUS
- J10: footprint Connector_FFC-FPC:Hirose_FH12-40S-0.5SH_1x40-1MP_P0.50mm_Horizontal -> atlas:J_SMD_4-1734839-0-40_0.5_25.43_5.1_2.05
- J3: footprint Connector_FFC-FPC:Hirose_FH12-6S-0.5SH_1x06-1MP_P0.50mm_Horizontal -> atlas:TE_2328702-6
- J5: footprint Connector_PinHeader_1.27mm:PinHeader_1x03_P1.27mm_Vertical -> Connector_PinHeader_1.00mm:PinHeader_1x03_P1.00mm_Vertical
- R1: value 1k -> 10k; footprint Resistor_SMD:R_0603_1608Metric -> Resistor_SMD:R_0402_1005Metric
- R10: value NP -> 1k
- R18: value NP -> 1l
- R3: value 0 -> 100k; moved to F.Cu
- R33: value NP -> 100k
- R82, R83, R84: footprint Resistor_SMD:R_0603_1608Metric -> Jumper:SolderJumper-2_P1.3mm_Open_TrianglePad1.0x1.5mm
- SW1, SW4: footprint Button_Switch_SMD:SW_SPST_PTS645 -> Button_Switch_SMD:SW_SPST_PTS810
- SW2: value ResetNCP -> BTN_BOOT; footprint Button_Switch_SMD:SW_SPST_PTS645 -> Button_Switch_SMD:SW_SPST_PTS810; moved to F.Cu
- SW3: footprint Button_Switch_SMD:SW_SPST_PTS645 -> Button_Switch_SMD:SW_SPST_PTS810; moved to F.Cu
- SW5: value BTN_PWR -> ResetNCP; footprint Button_Switch_SMD:SW_SPST_PTS645 -> Button_Switch_SMD:SW_SPST_PTS810
- SW7: value NP -> BTN_C; footprint Button_Switch_SMD:SW_SPST_PTS645 -> Button_Switch_SMD:SW_SPST_PTS810
- U7: value MCP1810 -> EYSHSNZWZ; footprint Package_DFN_QFN:DFN-8-1EP_2x2mm_P0.5mm_EP0.9x1.5mm -> atlas:XCVR_EYSHSNZWZ; moved to F.Cu
- Y4: footprint Crystal:Crystal_SMD_3215-2Pin_3.2x1.5mm -> Crystal:Crystal_SMD_MicroCrystal_CC7V-T1A-2Pin_3.2x1.5mm; moved to F.Cu
- moved C27 160.8 mm to (45.7, 148.2), turned to 180 degrees
- moved R42 153.9 mm to (41.3, 132.6), turned to 270 degrees
- moved C38 153.0 mm to (39.6, 132.1), turned to 90 degrees
- moved R28 139.9 mm to (54.2, 136.2), turned to 180 degrees
- moved R29 139.2 mm to (54.3, 134.3), turned to 180 degrees
- moved D9 135.9 mm to (36.8, 119.2)
- moved C2 132.6 mm to (51.5, 115.0), turned to 0 degrees
- moved R19 128.2 mm to (43.4, 140.5), turned to 270 degrees
- moved C18 128.2 mm to (45.5, 151.9), turned to 180 degrees
- moved C6 124.6 mm to (63.7, 115.6)
- moved C46 121.6 mm to (59.5, 135.4), turned to 90 degrees
- moved R1 121.5 mm to (56.9, 103.3), turned to 270 degrees
- moved C24 121.3 mm to (69.8, 134.5), turned to 180 degrees
- moved C25 119.4 mm to (66.1, 123.8), turned to 180 degrees
- moved R48 117.4 mm to (42.0, 137.9)
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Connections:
- net /SDMMC1_CKIN_PB8 renamed /SDMMC1_CKIN
- net /SDMMC1_VSEL_PD1 renamed /SD_VSEL
- C11 pad 1: Net-(C11-Pad1) -> /VCC_3V3_MCU
- C12 pad 1: /VCAP2_STM -> /VCAP2
- C14 pad 1: /VCAP2_STM -> /VCAP2
- C2 pad 2: /VCC_3V3_PERIPH -> /VCC_3V3_MCU
- C20 pad 1: /VCC_3V3_PERIPH -> /VCC_3V3_MCU
- C31 pad 2: /USB_PORT_VBUS -> /VCC_SYS
- C35 pad 1: /USB_PORT_VBUS -> /VCC_SYS
- C37 pad 2: /USB_PORT_VBUS -> /VCC_SYS
- C38 pad 1: /VCC_3V3_PERIPH -> /VCC_3V3_MCU
- C4 pad 1: /VCAP1_STM -> /VCAP1
- C46 pad 1: /VCC_3V3_PERIPH -> /VCC_3V3_MCU
- C5 pad 1: /VCAP1_STM -> /VCAP1
- C50 pad 1: /VCC_3V3_PERIPH -> /VCC_3V3_MCU
- C54 pad 1: /VCC_3V3_PERIPH -> /VCC_3V3_MCU
- C56 pad 2: /VCC_3V3_PERIPH -> /VCC_3V3_MCU
- C57 pad 2: /VCC_3V3_PERIPH -> /VCC_3V3_MCU
- C58 pad 2: /VCC_3V3_PERIPH -> /VCC_3V3_MCU
- C59 pad 1: /VCC_3V3_PERIPH -> /VCC_3V3_MCU
- C61 pad 1: /VCC_3V3_PERIPH -> /VCC_3V3_MCU
- C7 pad 1: /USB_PORT_VBUS -> /VCC_SYS
- C8 pad 2: /USB_PORT_VBUS -> /VCC_SYS
- C9 pad 1: Net-(C9-Pad1) -> /VCC_3V3_MCU
- D1 pad 1: Net-(D1-Pad1) -> GND
- D1 pad 2: /GPS_1PPS -> Net-(D1-Pad2)
- D2 pad 1: Net-(D2-Pad1) -> GND
- D2 pad 2: /GPS_3DF -> Net-(D2-Pad2)
- D3 pad 1: Net-(D3-Pad1) -> /CHG_STATUS
- D3 pad 2: /VCC_BACKUP -> Net-(D3-Pad2)
- D4 pad 1: Net-(D4-Pad1) -> GND
- D4 pad 2: /VCC_3V3 -> Net-(D4-Pad2)
- D6 pad 1: /VCC_3V3_MCU_EN -> /MCU_3V3_EN
- D6 pad 2: /SW_PWR -> /SW_C_PWR
- D7 pad 1: Net-(D7-Pad1) -> GND
- D7 pad 2: /USB_PORT_VBUS -> Net-(D7-Pad2)
- D9 pad 1: Net-(D9-Pad1) -> GND
- D9 pad 2: /VCC_3V3_MCU -> Net-(D9-Pad2)
- J10 pad 37: /VCC_3V3_PERIPH -> /VCC_3V3_MCU
- J10 pad 38: /VCC_3V3_PERIPH -> /VCC_3V3_MCU
- J3 pad 1: /I2C4_SCL_SENSOR_PB6 -> /I2C4_SCL_SENSOR
- J3 pad 2: /I2C4_SCL_SENSOR_PB7 -> /I2C4_SDA_SENSOR
- J3 pad 4: /VCC_MCU_3V3 -> /VCC_3V3_MCU
- J3 pad 6: /DEBUG_NRESET_STM -> Net-(J3-Pad6)
- L10 pad 1: /USB_PORT_VBUS -> /VCC_SYS
- L2 pad 1: /USB_PORT_VBUS -> /VCC_SYS
- L4 pad 2: /USB_PORT_VBUS -> /VCC_SYS
- R1 pad 1: Net-(D9-Pad1) -> /VCC_BACKUP
- R1 pad 2: /PERIPH_FAULT -> Net-(Q1-Pad5)
- R10 pad 1: /USB_PORT_VBUS -> /NCP_STATUS
- R10 pad 2: Net-(C9-Pad1) -> Net-(D9-Pad2)
- R18 pad 1: /JOY_Y -> /STM_STATUS_C
- R2 pad 1: Net-(D2-Pad1) -> /GPS_3DF
- R2 pad 2: GND -> Net-(D2-Pad2)
- R20 pad 1: Net-(J9-Pad4) -> Net-(J9-Pad1)
- R28 pad 1: /VCC_3V3_PERIPH -> /VCC_3V3
- R28 pad 2: /I2C4_SCL_SENSOR_PB6 -> /I2C4_SCL_SENSOR
- R29 pad 1: /VCC_3V3_PERIPH -> /VCC_3V3
- R29 pad 2: /I2C4_SDA_SENSOR_PB7 -> /I2C4_SDA_SENSOR
- R3 pad 1: GND -> /VCC_3V3_MCU
- R3 pad 2: Net-(R3-Pad2) -> Net-(J3-Pad6)
- R33 pad 1: /VCC_3V3_MCU -> /SW_C_PWR
- R33 pad 2: /JOY_X -> GND
- R4 pad 1: /VCC_MCU_3V3 -> /SW_BOOT
- R4 pad 2: /SW_BOOT -> GND
- R40 pad 1: /VCC_MCU_3V3 -> /SW_L
- R40 pad 2: /SW_L -> GND
- R42 pad 1: /VCC_3V3_PERIPH -> /VCC_3V3
- R44 pad 1: Net-(C42-Pad2) -> Net-(Q1-Pad3)
- R47 pad 2: /T3C1_LCD_BL -> /T2C4_LCD_BL
- R48 pad 1: /VCC_MCU_3V3 -> /SW_R
- R48 pad 2: /SW_R -> GND
- R49 pad 1: /VCC_3V3_PERIPH -> /VCC_3V3
- R51 pad 1: Net-(C28-Pad1) -> Net-(AE1-Pad1)
- R55 pad 2: /VCC_3V3_PERIPH -> /VCC_3V3_MCU
- R6 pad 1: Net-(D3-Pad1) -> /USB_PORT_VBUS
- R6 pad 2: /CHG_STATUS -> Net-(D3-Pad2)
- R8 pad 1: Net-(D4-Pad1) -> /VCC_3V3_MCU
- R8 pad 2: GND -> Net-(D4-Pad2)
- R87 pad 1: Net-(D7-Pad1) -> /USB_PORT_VBUS
- R87 pad 2: GND -> Net-(D7-Pad2)
- R9 pad 1: Net-(D1-Pad1) -> /GPS_1PPS
- R9 pad 2: GND -> Net-(D1-Pad2)
- SW1 pad 1: /SW_L -> /VCC_MCU_3V3
- SW1 pad 2: GND -> /SW_L
- SW2 pad 1: /DEBUG_NRESET_NCP -> /VCC_MCU_3V3
- SW2 pad 2: GND -> /SW_BOOT
- SW4 pad 1: /SW_R -> /VCC_MCU_3V3
- SW4 pad 2: GND -> /SW_R
- SW5 pad 1: /VCC_BACKUP -> /DEBUG_NRESET_NCP
- SW5 pad 2: /SW_PWR -> GND
- SW7 pad 1: /JOY_X -> /VCC_MCU_3V3
- SW7 pad 2: GND -> /SW_C_PWR
- U1 pad 25: /STM_STATUS_R -> /T2C4_LCD_BL
- U1 pad 32: /LCD_REG_EN -> /STM_STATUS_R
- U1 pad 48: /VCAP1_STM -> /VCAP1
- U1 pad 57: /PERIPH_REG_EN -> /LCD_REG_EN
- U1 pad 70: /USB_STM_D- -> /USB_PORT_D-
- U1 pad 71: /USB_STM_D+ -> /USB_PORT_D+
- U1 pad 73: /VCAP2_STM -> /VCAP2
- U1 pad 81: /SDMMC1_DET -> /SD_DET
- U1 pad 90: /T3C1_LCD_BL -> /GYRO_INT
- U1 pad 97: /SPI4_NCS_ACCEL -> /SPI4_ACCEL_NCS
- U1 pad 98: /SPI4_NCS_GYRO -> /SPI4_GYRO_NCS
- U10 pad 7: /I2C4_SCL_SENSOR_PB6 -> /I2C4_SCL_SENSOR
- U10 pad 8: /I2C4_SDA_SENSOR_PB7 -> /I2C4_SDA_SENSOR
- U11 pad 23: /VCC_3V3_PERIPH -> /VCC_3V3_MCU
- U11 pad 30: Net-(U11-Pad30) -> Net-(Q1-Pad2)
- U11 pad 7: /GPS_EXTINT -> /GPS_INT
- U11 pad 9: /VCC_3V3_PERIPH -> /VCC_3V3_MCU
- U12 pad 1: Net-(J9-Pad4) -> Net-(J9-Pad1)
- U12 pad 5: /T3C1_LCD_BL -> /T2C4_LCD_BL
- U12 pad 6: /USB_PORT_VBUS -> /VCC_SYS
- U14 pad 1: /VCC_3V3_PERIPH -> /VCC_3V3_MCU
- U14 pad 2: /I2C4_SDA_SENSOR_PB7 -> /I2C4_SDA_SENSOR
- U14 pad 3: /I2C4_SCL_SENSOR_PB6 -> /I2C4_SCL_SENSOR
- U18 pad 1: /VCC_3V3_PERIPH -> /VCC_3V3_MCU
- U18 pad 14: /VCC_3V3_PERIPH -> /VCC_3V3_MCU
- U2 pad B4: /VCC_3V3_PERIPH -> /VCC_3V3_MCU
- U2 pad D1: /VCC_3V3_PERIPH -> /VCC_3V3_MCU
- U2 pad E4: /VCC_3V3_PERIPH -> /VCC_3V3_MCU
- U3 pad 7: /USB_PORT_VBUS -> /VCC_SYS
- U3 pad 8: /USB_PORT_VBUS -> /VCC_SYS
- U4 pad 1: /VCC_3V3_MCU_EN -> /MCU_3V3_EN
- U4 pad 4: /USB_PORT_VBUS -> /VCC_SYS
- U5 pad 8: /VCC_3V3_PERIPH -> /VCC_3V3_MCU
- U6 pad 2: Net-(C9-Pad1) -> /VCC_3V3_MCU
- U6 pad 8: Net-(R3-Pad2) -> GND
- U7 pad 2: Net-(C42-Pad2) -> Net-(U7-Pad2)
- U7 pad 6: Net-(C42-Pad2) -> Net-(U7-Pad6)
- U7 pad 7: /VCC_3V3_PERIPH -> Net-(U7-Pad7)
- U7 pad 8: Net-(U11-Pad30) -> /VCC_3V3_MCU
- U7 pad 9: GND -> Net-(U7-Pad9)
- U8 pad 6: /USB_PORT_VBUS -> /VCC_SYS
- U9 pad 15: /USB_PORT_VBUS -> /VCC_SYS
- U9 pad 16: /USB_PORT_VBUS -> /VCC_SYS
- Y1 pad 2: /RCC_OSC_IN -> GND
- Y1 pad 3: (no net) -> /RCC_OSC_IN
- Y1 pad 4: (no net) -> GND
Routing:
- net /LTDC_VS: track 33.5 -> 8.36 mm, vias 2 -> 0
- net /LCD_REG_EN: track 19.7 -> 0.00 mm, vias 2 -> 0
- net /USB_STM_D+: track 19.7 -> 0.00 mm
- net /USB_STM_D-: track 20.4 -> 2.71 mm
- net /VCC_SYS: track 0.00 -> 14.7 mm
- net GND: track 0.00 -> 13.4 mm, vias 38 -> 21
- net Net-(C28-Pad1): track 12.4 -> 0.00 mm
- net /I2C4_SDA_SENSOR: track 0.00 -> 12.3 mm, vias 0 -> 1
- net /CELL_POS: track 0.00 -> 12.1 mm
- net /LTDC_CK: track 27.4 -> 15.8 mm, vias 1 -> 0
- net /LTDC_DE: track 26.9 -> 15.4 mm, vias 1 -> 0
- net /OCTOSPIM_P1_NCS: track 0.00 -> 10.5 mm, vias 0 -> 2
- net /VCC_LCD_PWR: track 0.00 -> 10.3 mm, vias 0 -> 1
- net /LTDC_HS: track 32.6 -> 22.4 mm
- net /I2C4_SCL_SENSOR: track 0.00 -> 10.1 mm, vias 0 -> 1
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- added copper zone on In2.Cu, net /VCC_3V3_MCU
- added copper zone on F.Cu, net GND
- added copper zone on In1.Cu, net GND
- added copper zone on F.Cu, net Net-(D11-Pad2)
- removed copper zone on B.Cu, net Net-(D11-Pad2)
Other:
- board size 80 x 60 mm -> 70 x 70 mm
